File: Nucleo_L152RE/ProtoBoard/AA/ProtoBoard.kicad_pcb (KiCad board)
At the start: 2 copper layers, 68.6 x 80.5 mm, 115 parts, among them CON1 USB-MICRO-B, J1 EXT1, J2 EXT2, J3 EXTPower, P1 Power, P10 OW2_A, P11 GND1, P12 I2C1_B, P13 I2C2_B, P14 SW_1_6, P15 WS1, P16 WS2, P17 MS2, P18 WS3, P19 WS4, P2 VinPower, P20 GND2, P21 Hole, P22 MS3, P23 OW3_A, P24 OW4_A, P25 MS4, P26 Hole, P27 Hole, P28 RGB1, P29 Ant, P3 USART2, P30 Hole, P4 SWD Header, P5 USART1, P6 MS1, P7 I2C1_A, P8 I2C2_A, P9 OW1_A, Q1 SI2323DS, SW1 MomentarySwitch, U2 Nucleo-L152RE-CN7, U3 Nucleo-L152RE-CN10, U5 MT3329_GPS, U6 S25FL127S, U7 RFM69HW

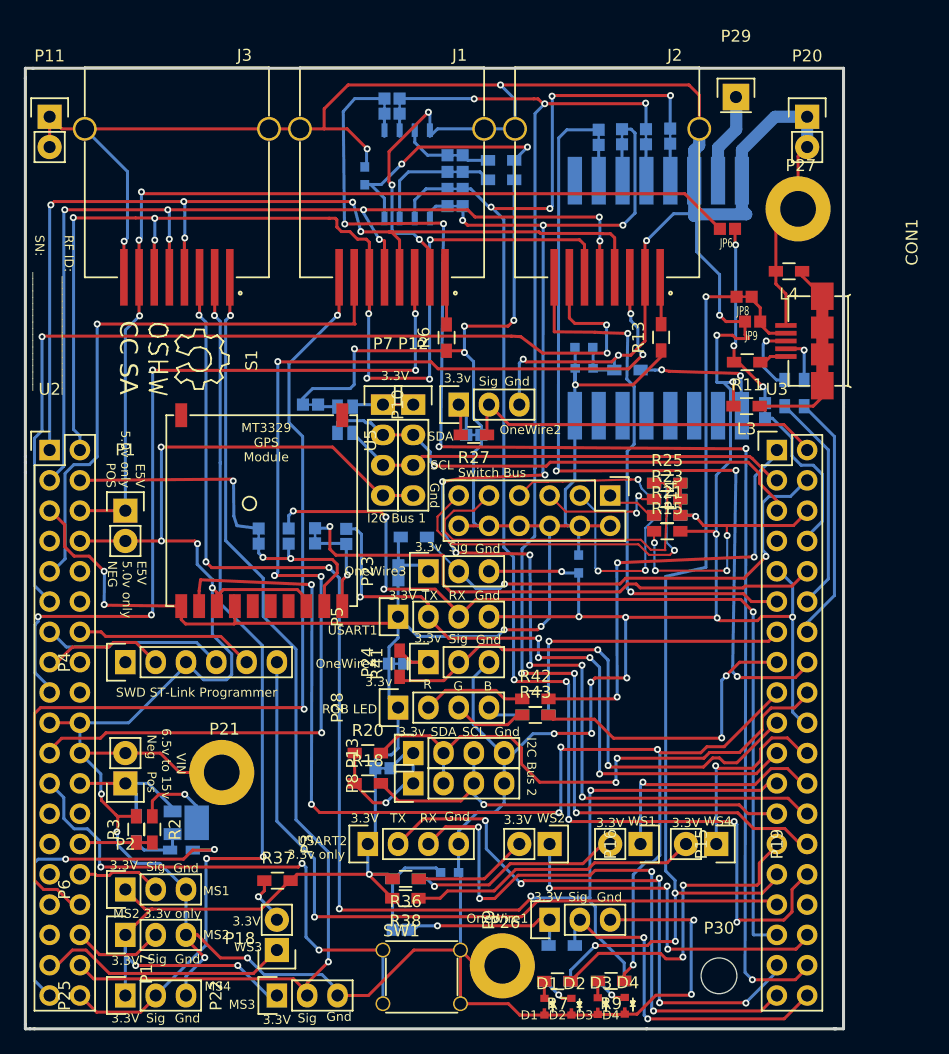
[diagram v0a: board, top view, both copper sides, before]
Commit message: Ground plane implemented on 2 layers.
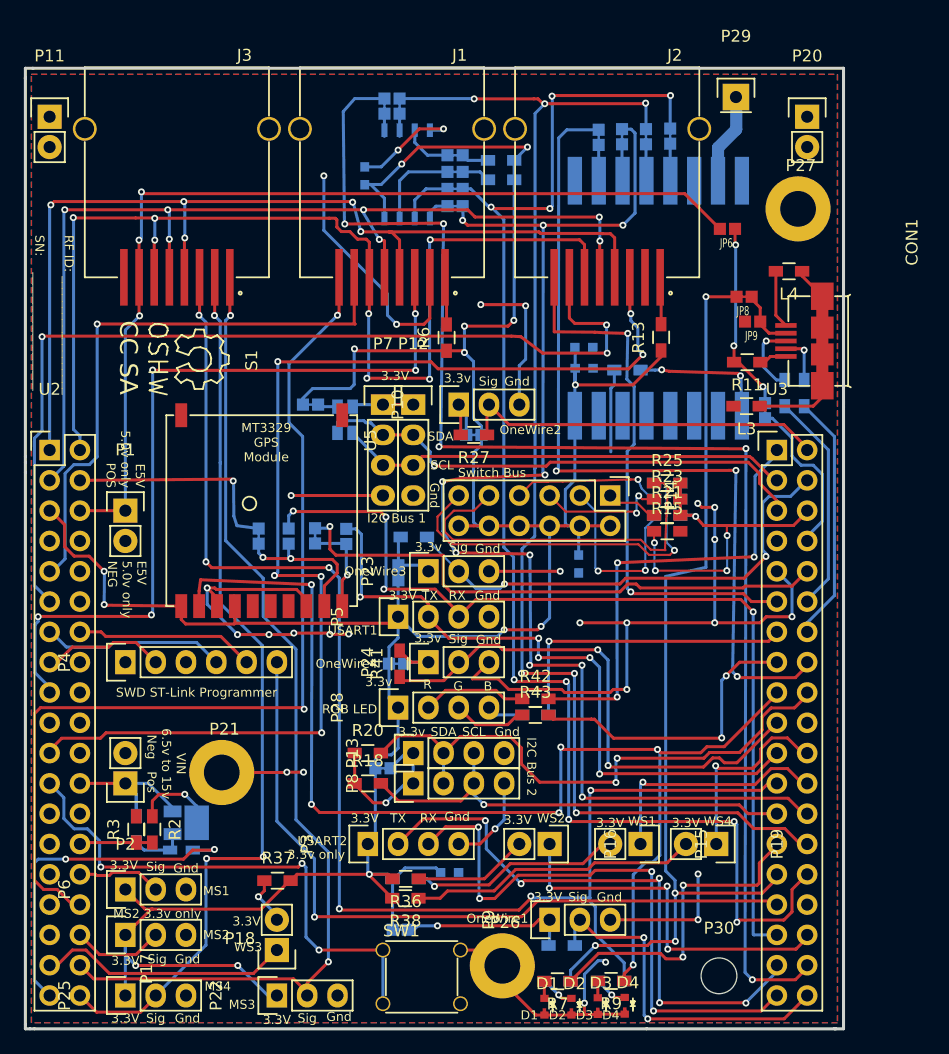
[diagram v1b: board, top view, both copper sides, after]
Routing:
- net GND: track 536.2 -> 210.3 mm, vias 32 -> 29
- added copper zone on B.Cu, net GND
- added copper zone on F.Cu, net GND

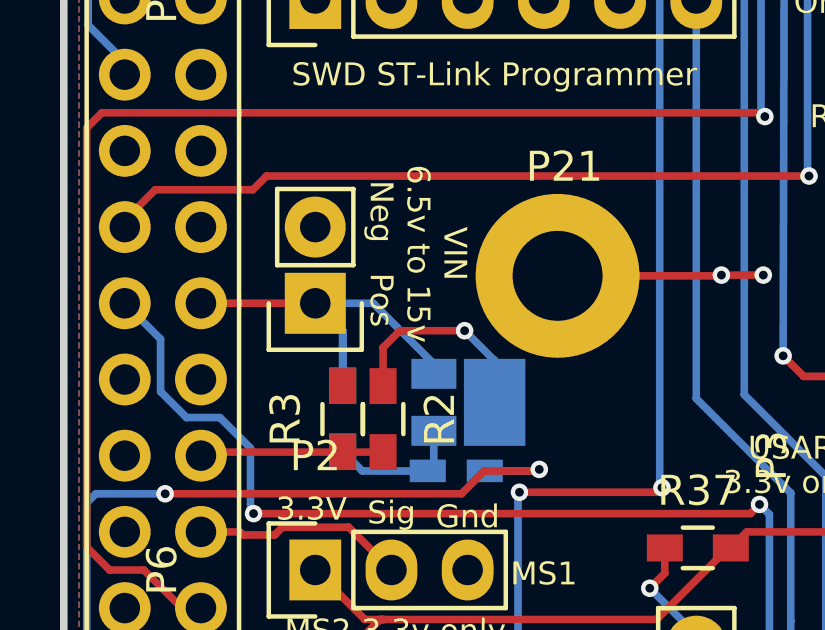
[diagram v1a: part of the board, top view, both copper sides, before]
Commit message: Submitted first printing of AA version. Uploading Gerbers since we would like to be able to get back to this point.
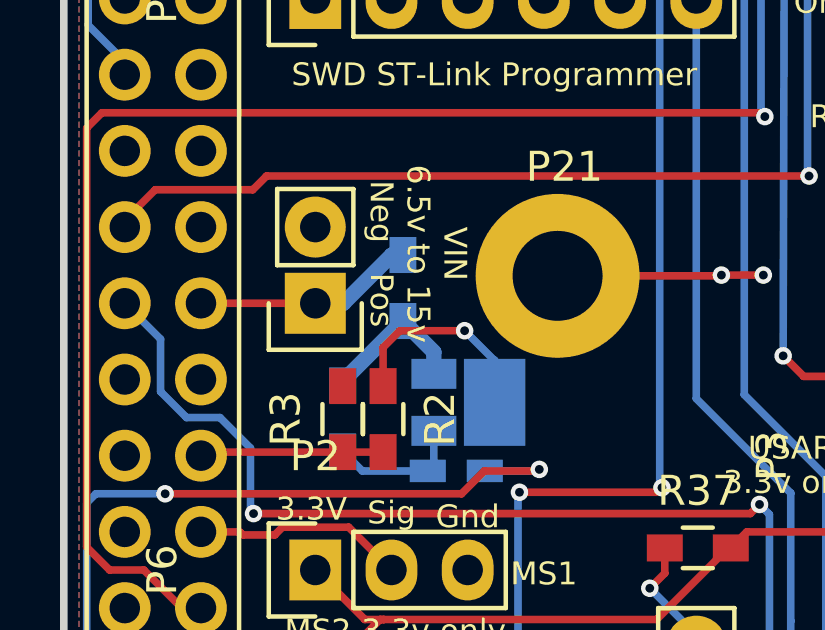
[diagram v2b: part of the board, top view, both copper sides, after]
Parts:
- added R4: 0, Resistors_SMD:R_0603_HandSoldering, B.Cu at (133.7, 107.4)
- C9: value 0.1p -> 0.1u
- R2: value 4.7k 1% -> 2.20k 1%
- R3: value 6.8k 1% -> 8.66k 1%
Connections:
- Q1 pad 2: +15V -> Net-(Q1-Pad2)
- R1 pad 1: +15V -> Net-(Q1-Pad2)
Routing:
- net +15V: track 16.5 -> 7.40 mm
- net Net-(Q1-Pad2): track 0.00 -> 5.49 mm
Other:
- board text added: "YMD: 20150410"
- board text removed: "YMD: 20150405"

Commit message: Adding notes to schematic and board layout to indicate the very broken wireless module interface.  New board will need to be created to fix the issue.
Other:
- board text added: "Note: 3 components under RFM module"
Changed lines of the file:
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@@
     (area 116.113571 44.194 202.137628 130.05526)
     (thickness 1.6)
-    (drawings 107)
+    (drawings 108)
     (tracks 1509)
     (zones 0)
@@
   )
   (setup
-    (last_trace_width 0.508)
+    (last_trace_width 0.254)
     (user_trace_width 0.1778)
     (user_trace_width 0.254)
@@
     (aux_axis_origin 0 0)
     (grid_origin 115.57 72.39)
-    (visible_elements 7FFEFF1F)
+    (visible_elements 7FFEFF7F)
     (pcbplotparams
       (layerselection 0x010fc_80000001)
@@
     )
   )
+  (gr_text "Note: 3 components under RFM module" (at 215.138 70.6628) (layer Dwgs.User)
+    (effects (font (size 1.5 1.5) (thickness 0.3)))
+  )
   (gr_text "MS2 3.3v only" (at 133.477 118.872) (layer F.SilkS)
